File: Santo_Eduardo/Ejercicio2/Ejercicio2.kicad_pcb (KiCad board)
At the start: 2 copper layers, 40.6 x 61 mm, 15 parts, among them J1 DB9, U1 AMIS42665TJAA1RG, U2 MAX232

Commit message: PCB Modo OpenGL
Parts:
- renumbered C1 to C11, C2 to C11, C3 to C11, C4 to C11, C5 to C11, C6 to C11, G102 to G1011, G101 to G1011, J1 to J11, JP1 to JP11, R1 to R11, R2 to R11, U1 to U11, U2 to U11, XA1 to XA11
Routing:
- net GND: track 229.8 -> 228.6 mm
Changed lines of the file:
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@@
     (links 44)
     (no_connects 0)
-    (area 126.543999 75.362999 167.334001 136.473001)
+    (area 120.475699 75.036699 167.334001 137.0941)
     (thickness 1.6)
     (drawings 6)
-    (tracks 242)
+    (tracks 243)
     (zones 0)
     (modules 15)
@@
   (module Ejercicio2:DB9_F_TH (layer F.Cu)
     (at 136.144 90.805 90)
-    (fp_text reference J1 (at -16.165 1.735 180) (layer F.SilkS)
+    (fp_text reference J11 (at -16.165 1.735 180) (layer F.SilkS)
       (effects (font (size 0.7112 0.4572) (thickness 0.1143)))
     )
@@
   (module Ejercicio2:CON_PALETA_3 (layer F.Cu)
     (at 129.794 113.538 90)
-    (fp_text reference JP1 (at -4.826 0 90) (layer F.SilkS)
+    (fp_text reference JP11 (at -4.826 0 90) (layer F.SilkS)
       (effects (font (size 0.762 0.4572) (thickness 0.127)))
     )
@@
     (tags "resistor 1206")
     (attr smd)
-    (fp_text reference R1 (at 4.572 0 90) (layer B.SilkS)
+    (fp_text reference R11 (at 4.572 0 90) (layer B.SilkS)
       (effects (font (size 1 1) (thickness 0.15)) (justify mirror))
     )
@@
     (tags "resistor 1206")
     (attr smd)
-    (fp_text reference R2 (at -4.572 0 270) (layer B.SilkS)
+    (fp_text reference R11 (at -4.572 0 270) (layer B.SilkS)
       (effects (font (size 1 1) (thickness 0.15)) (justify mirror))
     )
@@
     (at 147.066 115.443 180)
     (descr SO-8)
-    (fp_text reference U1 (at 0 -3.1 180) (layer F.SilkS)
+    (fp_text reference U11 (at 0 -3.1 180) (layer F.SilkS)
       (effects (font (size 0.7112 0.4572) (thickness 0.1143)))
     )
@@
     (tags "SMALL OUTLINE INTEGRATED CIRCUIT")
     (attr smd)
-    (fp_text reference U2 (at -4.3815 -5.0165 360) (layer F.SilkS)
+    (fp_text reference U11 (at -4.3815 -5.0165 360) (layer F.SilkS)
       (effects (font (size 0.762 0.762) (thickness 0.1143)))
     )
@@
     (at 159.004 81.788)
     (tags "CONN Poncho")
-    (fp_text reference XA1 (at -0.508 -2.032) (layer F.SilkS)
+    (fp_text reference XA11 (at -0.508 -2.032) (layer F.SilkS)
       (effects (font (size 0.7112 0.4572) (thickness 0.1143)))
     )
@@
   (module Ejercicio2:1206 (layer F.Cu)
     (at 147.066 110.998)
-    (fp_text reference C1 (at -4.826 0) (layer F.SilkS)
+    (fp_text reference C11 (at -4.826 0) (layer F.SilkS)
       (effects (font (size 1 1) (thickness 0.15)))
     )
@@
   (module Ejercicio2:1206 (layer F.Cu)
     (at 140.843 94.488 270)
-    (fp_text reference C2 (at -4.318 0 360) (layer F.SilkS)
+    (fp_text reference C11 (at -4.318 0 360) (layer F.SilkS)
       (effects (font (size 1 1) (thickness 0.15)))
     )
@@
   (module Ejercicio2:1206 (layer F.Cu)
     (at 140.843 101.6 270)
-    (fp_text reference C3 (at 4.318 0 540) (layer F.SilkS)
+    (fp_text reference C11 (at 4.318 0 540) (layer F.SilkS)
       (effects (font (size 1 1) (thickness 0.15)))
     )
@@
   (module Ejercicio2:1206 (layer F.Cu)
     (at 147.066 92.329 180)
-    (fp_text reference C4 (at -4.318 0 180) (layer F.SilkS)
+    (fp_text reference C11 (at -4.318 0 180) (layer F.SilkS)
       (effects (font (size 1 1) (thickness 0.15)))
     )
@@
   (module Ejercicio2:1206 (layer F.Cu)
     (at 147.066 95.25)
-    (fp_text reference C5 (at 4.318 0) (layer F.SilkS)
+    (fp_text reference C11 (at 4.318 0) (layer F.SilkS)
       (effects (font (size 1 1) (thickness 0.15)))
     )
@@
   (module Ejercicio2:1206 (layer F.Cu)
     (at 147.066 108.458)
-    (fp_text reference C6 (at -4.826 0) (layer F.SilkS)
+    (fp_text reference C11 (at -4.826 0) (layer F.SilkS)
       (effects (font (size 1 1) (thickness 0.15)))
     )
@@
   (module Ejercicio2:Logo_Poncho (layer F.Cu)
     (at 147.066 128.0795)
-    (fp_text reference G102 (at 0.127 5.588) (layer F.SilkS) hide
+    (fp_text reference G1011 (at 0.127 5.588) (layer F.SilkS) hide
       (effects (font (thickness 0.3)))
     )
@@
   (module Ejercicio2:Logo_OSHWA (layer F.Cu)
     (at 147.066 81.661)
-    (fp_text reference G101 (at 0 4.2418) (layer F.SilkS) hide
+    (fp_text reference G1011 (at 0 4.2418) (layer F.SilkS) hide
       (effects (font (size 0.7112 0.4572) (thickness 0.1143)))
     )
@@
   (gr_line (start 167.259 136.398) (end 126.619 136.398) (angle 90) (layer Edge.Cuts) (width 0.15))
   (gr_line (start 167.259 75.438) (end 167.259 136.398) (angle 90) (layer Edge.Cuts) (width 0.15))
+  (segment (start 131.699 109.093) (end 129.794 107.188) (width 0.3048) (layer F.Cu) (net 1))
+  (segment (start 129.794 107.188) (end 129.794 87.1855) (width 0.3048) (layer F.Cu) (net 1))
+  (segment (start 129.794 87.1855) (end 131.7117 85.2678) (width 0.3048) (layer F.Cu) (net 1))
+  (segment (start 131.7117 85.2678) (end 137.5664 85.2678) (width 0.3048) (layer F.Cu) (net 1))
   (via (at 163.957 83.185) (size 0.6) (drill 0.4) (layers F.Cu B.Cu) (net 1))
   (via (at 163.957 79.756) (size 0.6) (drill 0.4) (layers F.Cu B.Cu) (net 1))
@@
   (segment (start 134.493 109.093) (end 131.699 109.093) (width 0.3048) (layer F.Cu) (net 1))
   (segment (start 143.764 110.998) (end 141.859 109.093) (width 0.3048) (layer F.Cu) (net 1))
-  (segment (start 129.794 110.998) (end 129.794 87.1855) (width 0.3048) (layer F.Cu) (net 1))
-  (segment (start 129.794 87.1855) (end 131.7117 85.2678) (width 0.3048) (layer F.Cu) (net 1))
-  (segment (start 131.7117 85.2678) (end 137.5664 85.2678) (width 0.3048) (layer F.Cu) (net 1))
   (via (at 147.447 130.556) (size 0.6) (drill 0.4) (layers F.Cu B.Cu) (net 1))
   (via (at 144.8435 127.9525) (size 0.6) (drill 0.4) (layers F.Cu B.Cu) (net 1))
@@
   (segment (start 144.40408 106.3625) (end 142.5575 106.3625) (width 0.3048) (layer F.Cu) (net 12))
   (segment (start 142.5575 106.3625) (end 140.97 107.95) (width 0.3048) (layer F.Cu) (net 12))
-  (segment (start 140.97 107.95) (end 134.366 107.95) (width 0.3048) (layer F.Cu) (net 12))
-  (segment (start 134.366 107.95) (end 131.0005 104.5845) (width 0.3048) (layer F.Cu) (net 12))
-  (segment (start 131.0005 104.5845) (end 131.0005 92.626264) (width 0.3048) (layer F.Cu) (net 12))
+  (segment (start 140.97 107.95) (end 134.345336 107.95) (width 0.3048) (layer F.Cu) (net 12))
+  (segment (start 134.345336 107.95) (end 131.0005 104.605164) (width 0.3048) (layer F.Cu) (net 12))
+  (segment (start 131.0005 104.605164) (end 131.0005 92.626264) (width 0.3048) (layer F.Cu) (net 12))
   (segment (start 131.0005 92.626264) (end 131.0005 92.202) (width 0.3048) (layer F.Cu) (net 12))
   (segment (start 134.7216 92.1893) (end 131.0132 92.1893) (width 0.3048) (layer B.Cu) (net 12))
@@
   (segment (start 137.033 116.078) (end 142.113 116.078) (width 0.3048) (layer F.Cu) (net 14))
   (segment (start 142.113 116.078) (end 144.366 116.078) (width 0.3048) (layer F.Cu) (net 14))
+  (segment (start 129.794 113.538) (end 140.897803 113.538) (width 0.3048) (layer F.Cu) (net 15))
+  (segment (start 140.897803 113.538) (end 142.167803 114.808) (width 0.3048) (layer F.Cu) (net 15))
+  (segment (start 142.167803 114.808) (end 142.24 114.808) (width 0.3048) (layer F.Cu) (net 15))
+  (segment (start 142.24 114.808) (end 144.366 114.808) (width 0.3048) (layer F.Cu) (net 15))
   (segment (start 144.366 114.808) (end 146.3675 114.808) (width 0.3048) (layer F.Cu) (net 15))
   (segment (start 145.574 117.57) (end 144.399 117.57) (width 0.3048) (layer B.Cu) (net 15))
@@
   (via (at 146.3675 114.808) (size 0.6) (drill 0.4) (layers F.Cu B.Cu) (net 15))
   (segment (start 144.399 117.57) (end 144.399 116.713) (width 0.3048) (layer B.Cu) (net 15))
-  (segment (start 129.794 113.538) (end 137.414 113.538) (width 0.3048) (layer F.Cu) (net 15))
-  (segment (start 138.684 114.808) (end 142.24 114.808) (width 0.3048) (layer F.Cu) (net 15))
-  (segment (start 142.24 114.808) (end 144.366 114.808) (width 0.3048) (layer F.Cu) (net 15))
-  (segment (start 137.414 113.538) (end 138.684 114.808) (width 0.3048) (layer F.Cu) (net 15))
   (segment (start 149.606 113.57) (end 146.7805 113.57) (width 0.3048) (layer B.Cu) (net 16))
   (segment (start 146.7805 113.57) (end 146.685 113.4745) (width 0.3048) (layer B.Cu) (net 16))
@@
     (min_thickness 0.3048)
     (keepout (tracks allowed) (vias not_allowed) (copperpour not_allowed))
-    (fill (arc_segments 32) (thermal_gap 0.508) (thermal_bridge_width 0.508))
+    (fill yes (arc_segments 32) (thermal_gap 0.508) (thermal_bridge_width 0.508))
     (polygon
       (pts

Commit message: Added Stack-UP
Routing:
- net (no net): track 0.00 -> 7.87 mm
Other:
- board text added: "1 Oz"
- board text added: "1,6mm"
- board text added: "L1 Top (Mixed)"
- board text added: "L2 Bottom (Mixed)"
- board text added: "Stack-Up:"
- board text added: "Terminación superficial: HASL Espesor Final Aprox.: 1,6mm"
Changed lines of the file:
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@@
     (area 120.475699 75.036699 167.334001 137.0941)
     (thickness 1.6)
-    (drawings 6)
-    (tracks 243)
+    (drawings 19)
+    (tracks 244)
     (zones 0)
     (modules 15)
@@
   )
   (layers
-    (0 F.Cu signal)
-    (31 B.Cu signal)
-    (32 B.Adhes user)
-    (33 F.Adhes user)
+    (0 F.Cu mixed)
+    (31 B.Cu mixed)
     (34 B.Paste user)
     (35 F.Paste user)
@@
     (39 F.Mask user)
     (40 Dwgs.User user)
-    (41 Cmts.User user)
-    (42 Eco1.User user)
-    (43 Eco2.User user)
     (44 Edge.Cuts user)
     (45 Margin user)
     (46 B.CrtYd user)
     (47 F.CrtYd user)
-    (48 B.Fab user)
-    (49 F.Fab user)
   )
   (setup
@@
       (xy -2.42316 3.59156)) (layer F.SilkS) (width 0.00254))
   )
+  (gr_text "Terminación superficial: HASL\nEspesor Final Aprox.: 1,6mm" (at 175.768 108.712) (layer Dwgs.User)
+    (effects (font (size 1.5 1.5) (thickness 0.3)) (justify left))
+  )
+  (gr_text "L1 Top (Mixed)" (at 205.232 98.298) (layer Dwgs.User)
+    (effects (font (size 0.8 0.8) (thickness 0.2)))
+  )
+  (gr_text "L2 Bottom (Mixed)" (at 206.317715 103.124) (layer Dwgs.User)
+    (effects (font (size 0.8 0.8) (thickness 0.2)))
+  )
+  (gr_text "1 Oz" (at 175.768 103.124) (layer Dwgs.User)
+    (effects (font (size 0.8 0.8) (thickness 0.2)))
+  )
+  (gr_text "1 Oz" (at 175.768 98.298) (layer Dwgs.User)
+    (effects (font (size 0.8 0.8) (thickness 0.2)))
+  )
+  (gr_text 1,6mm (at 189.738 100.838) (layer Dwgs.User)
+    (effects (font (size 1.5 1.5) (thickness 0.3)))
+  )
+  (gr_line (start 191.77 103.124) (end 199.644 103.124) (layer Dwgs.User) (width 0.2))
+  (gr_line (start 188.722 103.124) (end 190.5 103.124) (layer Dwgs.User) (width 0.2))
+  (gr_line (start 179.578 103.124) (end 187.452 103.124) (layer Dwgs.User) (width 0.2))
+  (gr_line (start 191.77 98.298) (end 199.644 98.298) (layer Dwgs.User) (width 0.2))
+  (gr_line (start 188.722 98.298) (end 190.5 98.298) (layer Dwgs.User) (width 0.2))
+  (gr_line (start 179.578 98.298) (end 187.452 98.298) (layer Dwgs.User) (width 0.2))
+  (gr_text Stack-Up: (at 189.738 93.726) (layer Dwgs.User)
+    (effects (font (size 1.5 1.5) (thickness 0.3)))
+  )
   (gr_text "EHS\n1115" (at 152.527 134.747) (layer B.Cu)
     (effects (font (size 0.7 0.7) (thickness 0.175)) (justify mirror))
@@
   (gr_line (start 167.259 136.398) (end 126.619 136.398) (angle 90) (layer Edge.Cuts) (width 0.15))
   (gr_line (start 167.259 75.438) (end 167.259 136.398) (angle 90) (layer Edge.Cuts) (width 0.15))
+  (segment (start 178.308 98.552) (end 186.182 98.552) (width 0.3048) (layer Dwgs.User) (net 0))
   (segment (start 131.699 109.093) (end 129.794 107.188) (width 0.3048) (layer F.Cu) (net 1))
   (segment (start 129.794 107.188) (end 129.794 87.1855) (width 0.3048) (layer F.Cu) (net 1))

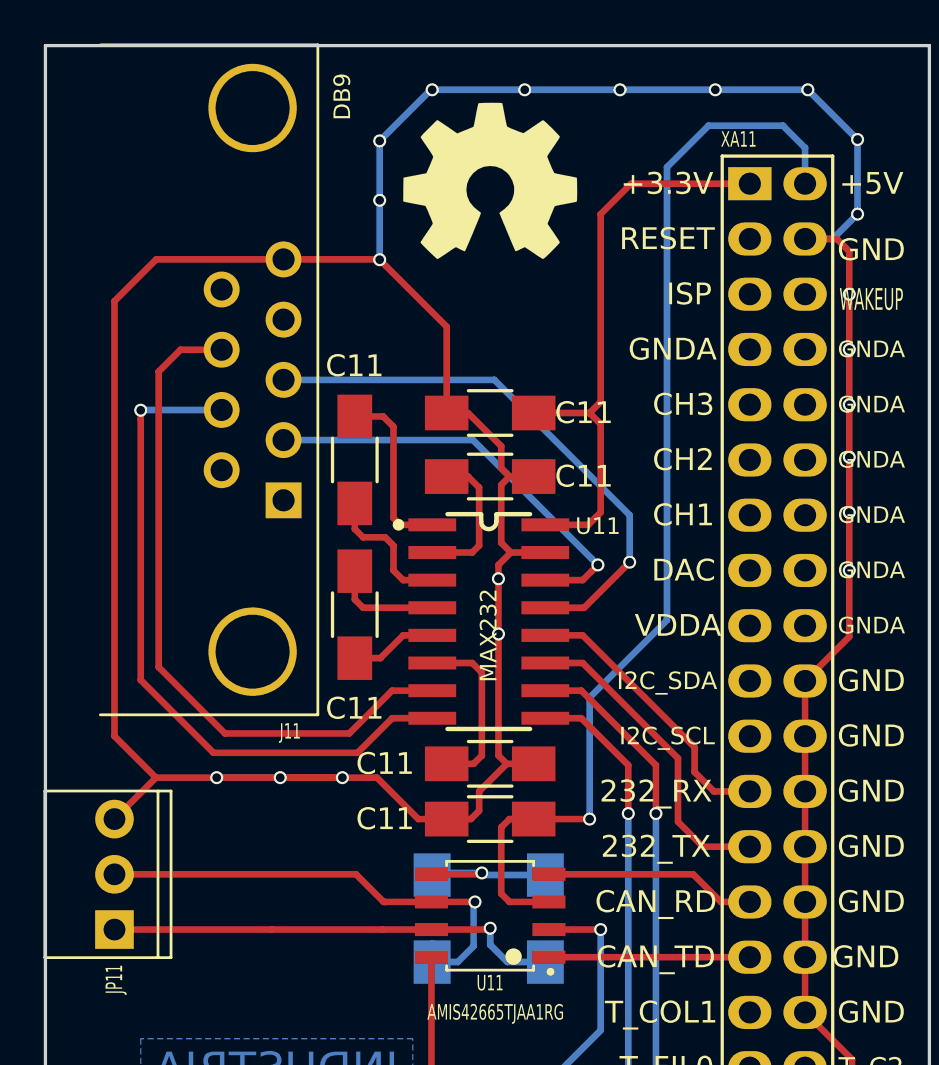
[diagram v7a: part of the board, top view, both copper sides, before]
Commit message: Probada característica lenght tunning.
Falló Kicad y no pude realizar el par diferencial
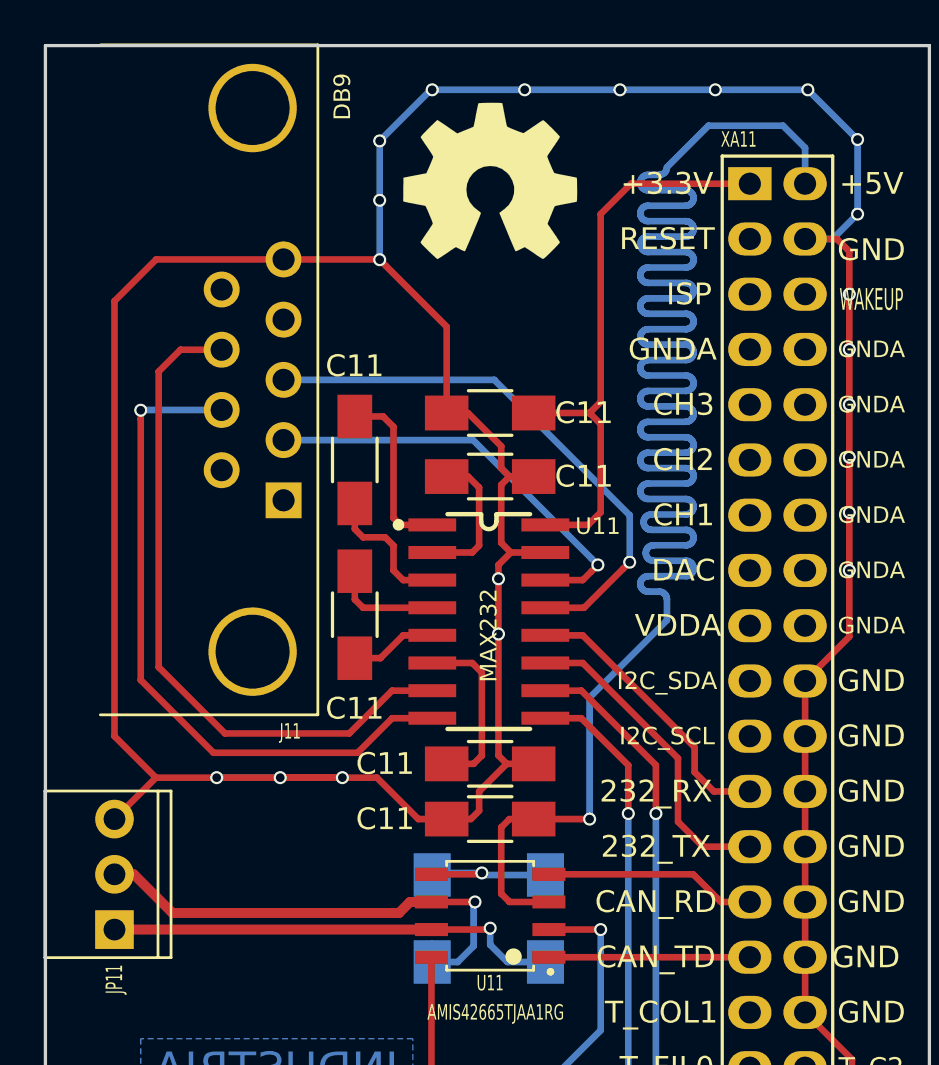
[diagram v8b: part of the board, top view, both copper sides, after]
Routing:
- net +5V: track 50.3 -> 107.0 mm
